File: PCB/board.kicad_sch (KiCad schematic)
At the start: 18 parts, among them SW1 SW_SPST, SW2 SW_Push, U1 STM32H743VITx, Y1 25 MHz

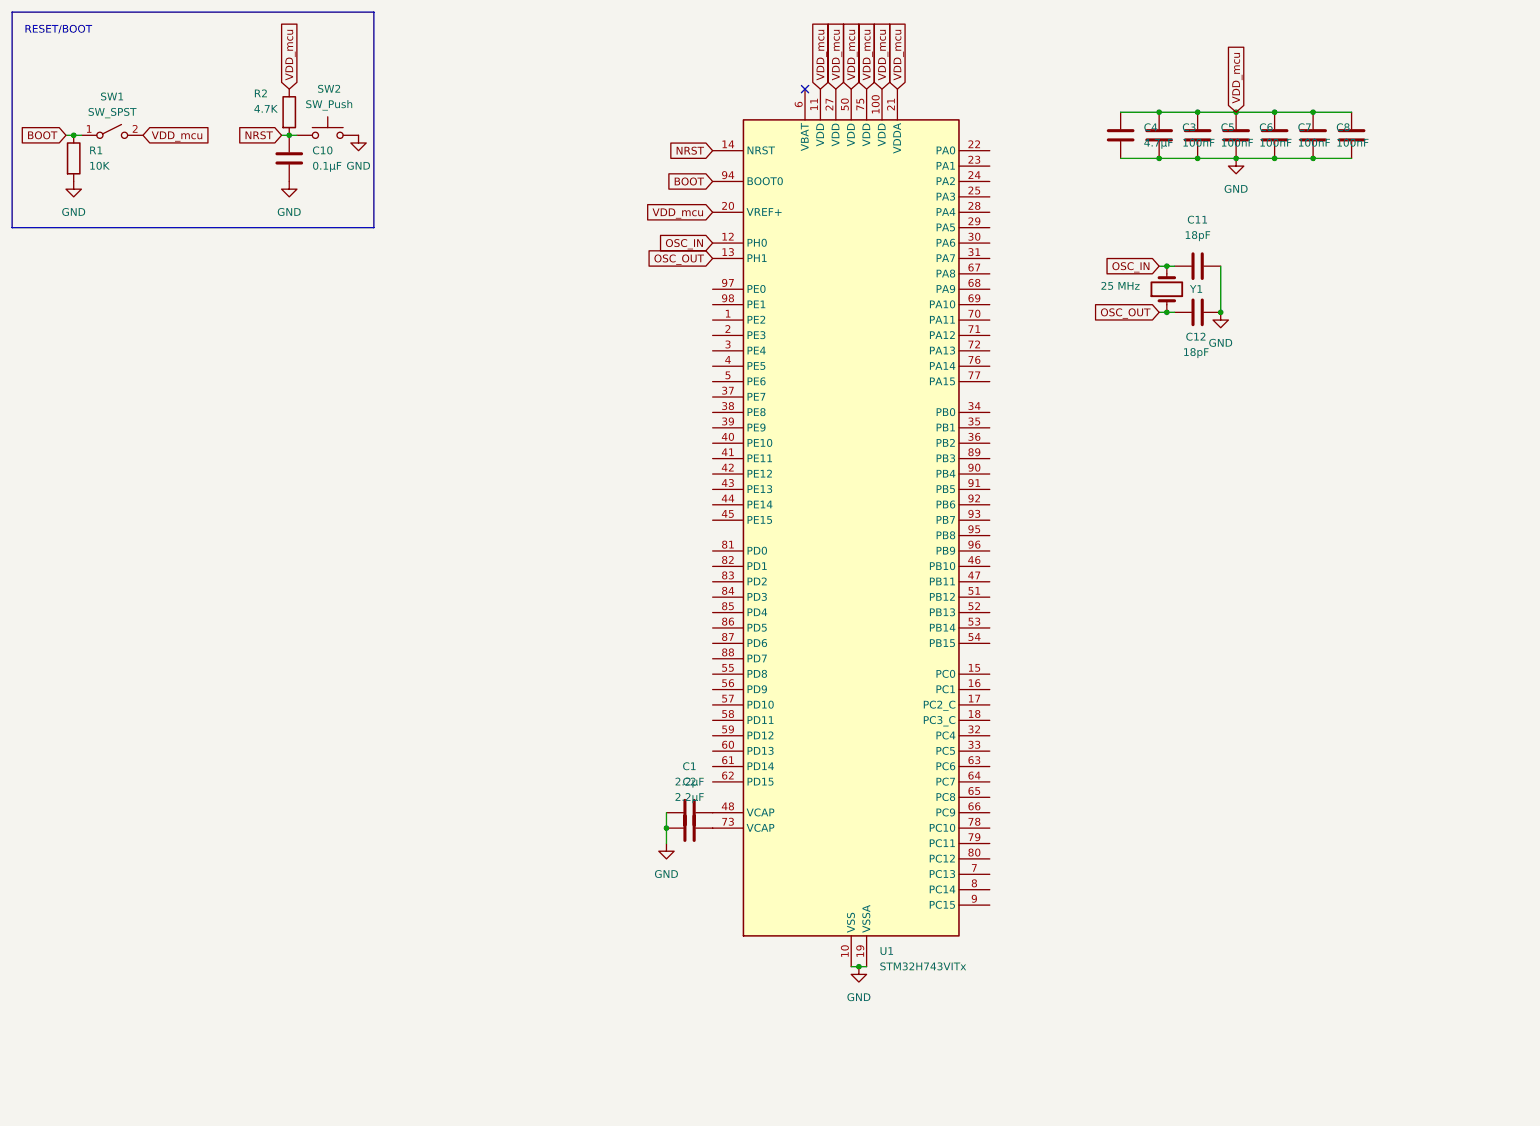
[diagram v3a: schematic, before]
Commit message: adding ferrite bead to VDD
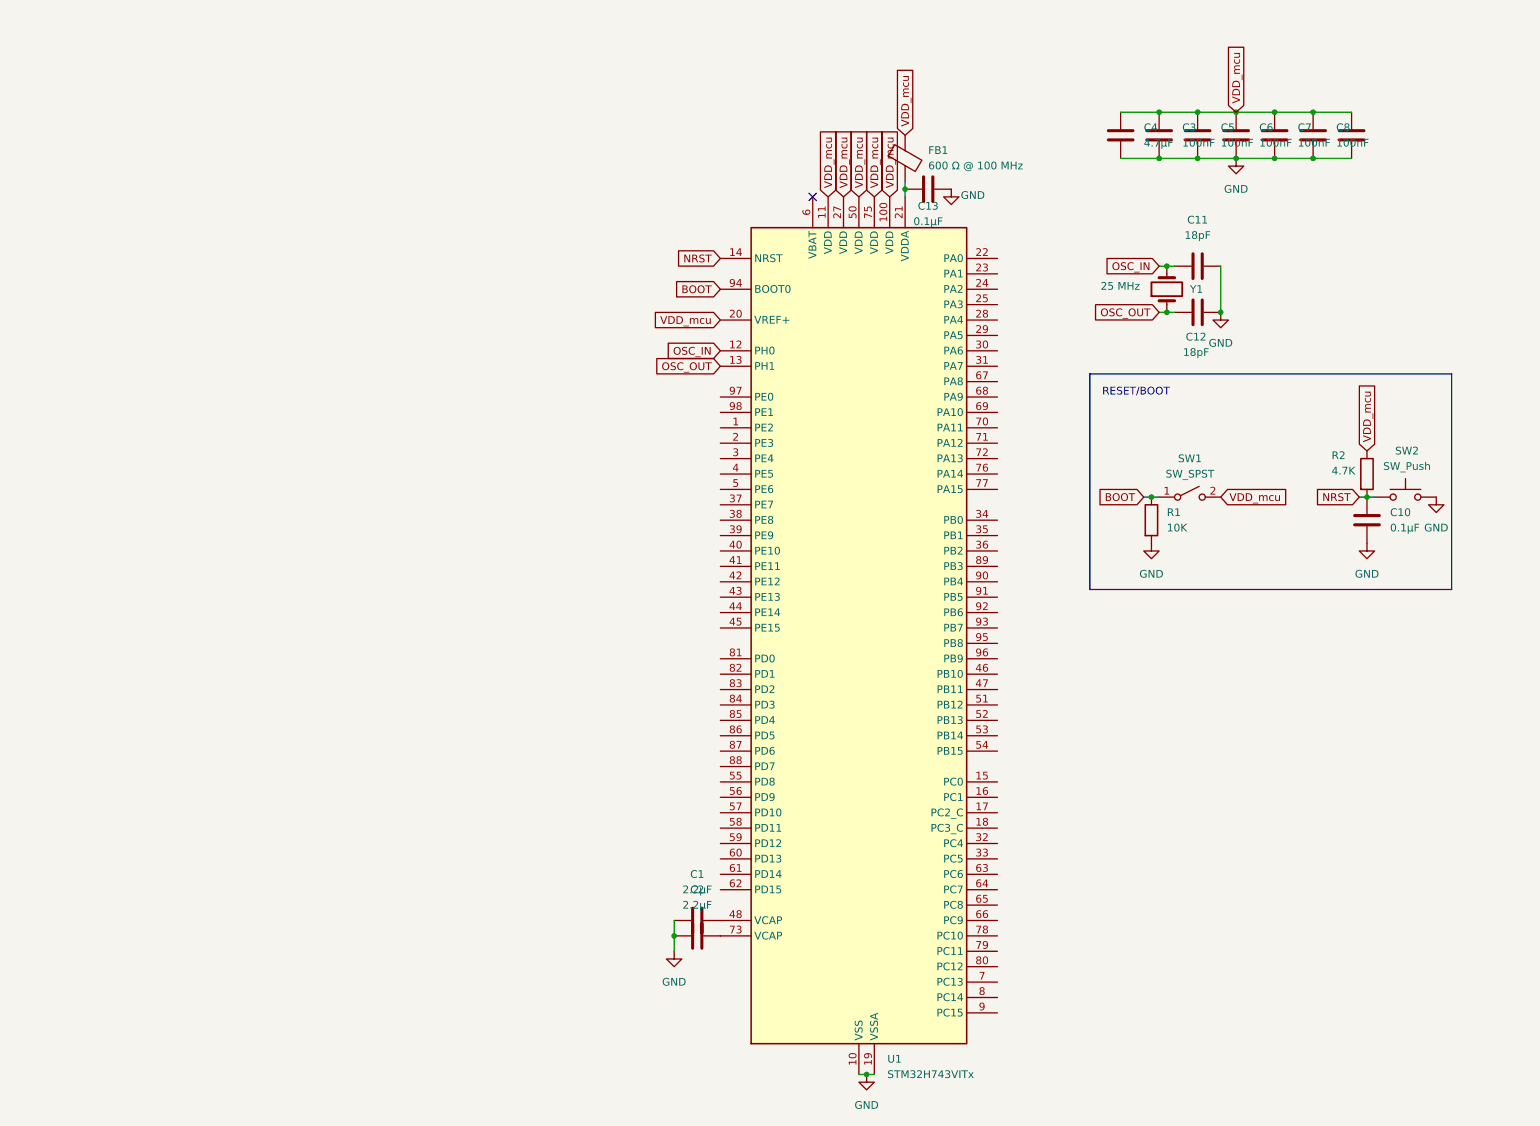
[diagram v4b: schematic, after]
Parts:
- added C13: 0.1µF, symbol Device:C
- added FB1: 600 Ω @ 100 MHz, symbol Device:FerriteBead
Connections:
- net GND: now also C13.2
- net VDD_mcu: now also FB1.1; no longer U1.21 (VDDA)
- new net: C13.1, FB1.2, U1.21 (VDDA)
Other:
- moved on the sheet: C1, C10, C2, R1, R2, SW1, SW2, U1

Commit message: adding my SWD debugger headers, I think I'm using the wrong symbol though
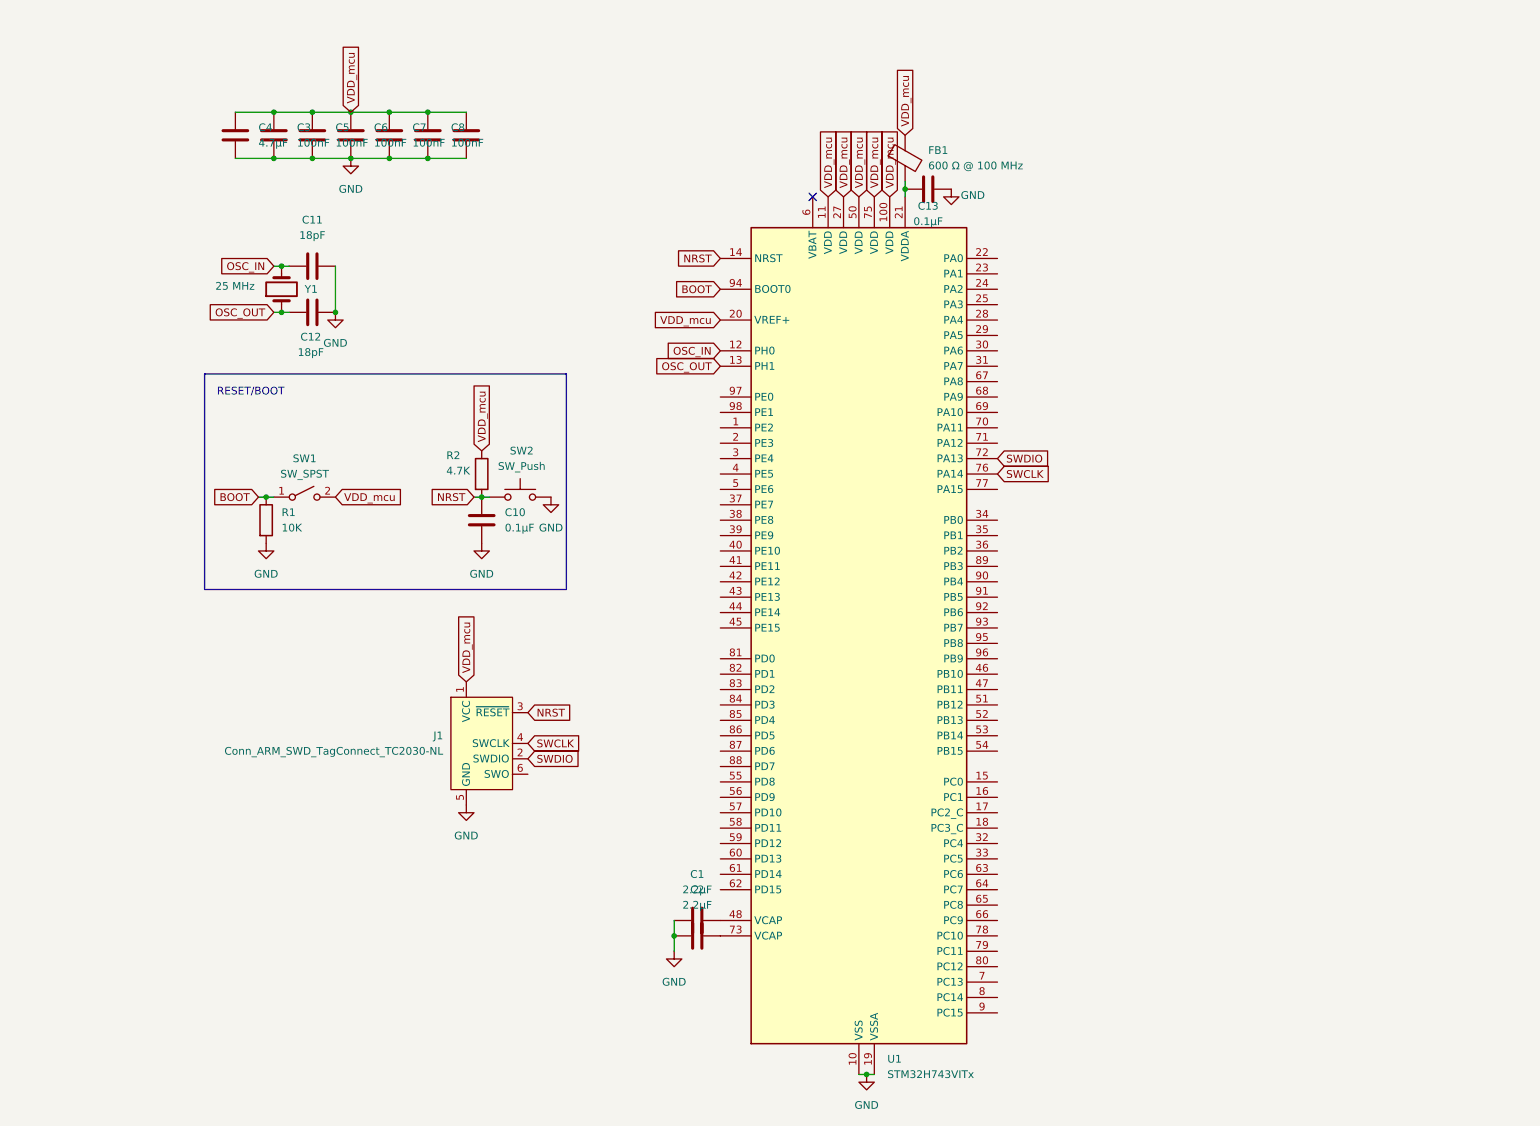
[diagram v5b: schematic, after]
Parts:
- added J1: Conn_ARM_SWD_TagConnect_TC2030-NL, Connector:Tag-Connect_TC2030-IDC-NL_2x03_P1.27mm_Vertical, symbol Connector:Conn_ARM_SWD_TagConnect_TC2030-NL
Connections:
- net GND: now also J1.5 (GND)
- net NRST: now also J1.3 (~{RESET})
- net VDD_mcu: now also J1.1 (VCC)
- net SWDIO: now reaches U1.72 (PA13)
- net SWDIO: now also J1.2 (SWDIO)
- net SWCLK: now reaches U1.76 (PA14)
- net SWCLK: now also J1.4 (SWCLK)
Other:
- moved on the sheet: C10, C11, C12, C3, C4, C5, C6, C7, C8, R1, R2, SW1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

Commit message: added the JTAG/SWD connector, and made it more detailed
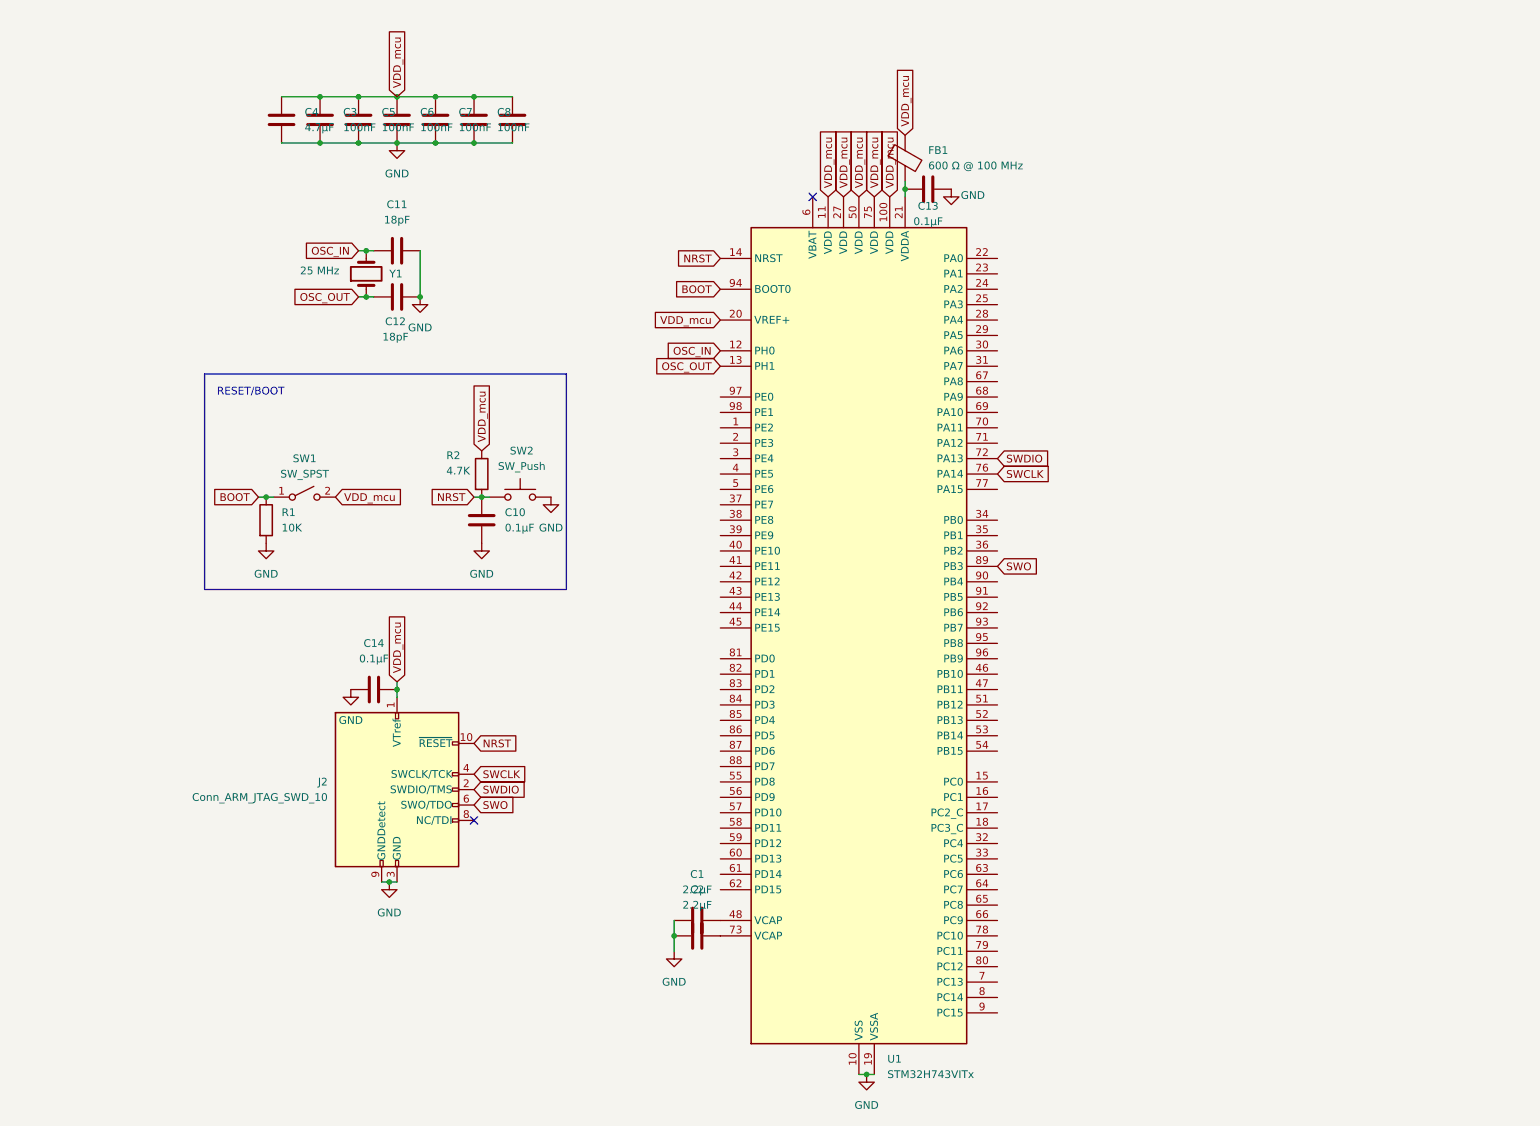
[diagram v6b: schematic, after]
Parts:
- removed J1: Conn_ARM_SWD_TagConnect_TC2030-NL, Connector:Tag-Connect_TC2030-IDC-NL_2x03_P1.27mm_Vertical, symbol Connector:Conn_ARM_SWD_TagConnect_TC2030-NL
- added C14: 0.1µF, symbol Device:C
- added J2: Conn_ARM_JTAG_SWD_10, symbol Connector:Conn_ARM_JTAG_SWD_10
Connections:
- net GND: now also C14.1, J2.3 (GND), J2.5 (GND), J2.9 (GNDDetect)
- net NRST: now also J2.10 (~{RESET})
- net SWCLK: now also J2.4 (SWCLK/TCK)
- net SWDIO: now also J2.2 (SWDIO/TMS)
- net VDD_mcu: now also C14.2, J2.1 (VTref)
- net SWO: now reaches U1.89 (PB3)
- net SWO: now also J2.6 (SWO/TDO)
- no-connect marks 1 -> 2
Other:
- moved on the sheet: C11, C12, C3, C4, C5, C6, C7, C8, Y1

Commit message: adding the SD card
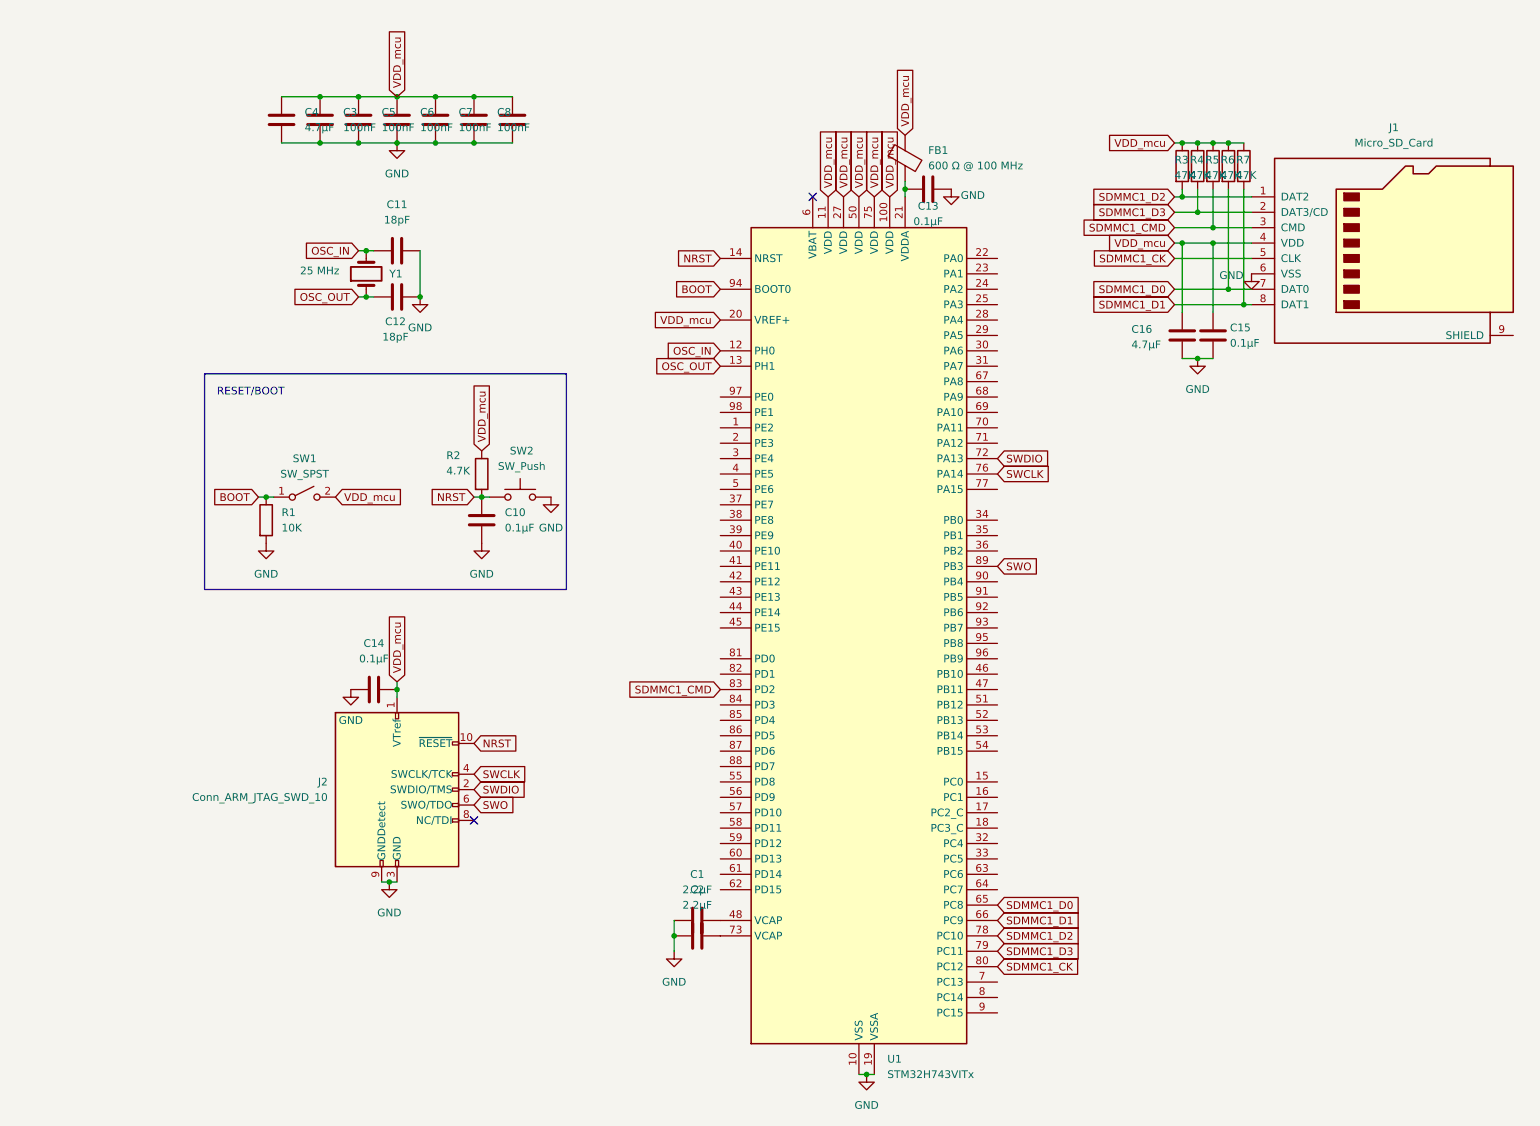
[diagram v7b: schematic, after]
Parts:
- added C15: 0.1µF, symbol Device:C
- added C16: 4.7µF, symbol Device:C
- added J1: Micro_SD_Card, symbol Connector:Micro_SD_Card
- added R3, R4, R5, R6, R7: 47K, symbol Device:R
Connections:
- net GND: now also C15.2, C16.2, J1.6 (VSS)
- net VDD_mcu: now also C15.1, C16.1, J1.4 (VDD), R3.1, R4.1, R5.1, R6.1, R7.1
- net SDMMC1_D0: now reaches U1.65 (PC8)
- net SDMMC1_D0: now also J1.7 (DAT0), R6.2
- net SDMMC1_D1: now reaches U1.66 (PC9)
- net SDMMC1_D1: now also J1.8 (DAT1), R7.2
- net SDMMC1_D2: now reaches U1.78 (PC10)
- net SDMMC1_D2: now also J1.1 (DAT2), R3.2
- net SDMMC1_D3: now reaches U1.79 (PC11)
- net SDMMC1_D3: now also J1.2 (DAT3/CD), R4.2
- net SDMMC1_CK: now reaches U1.80 (PC12)
- net SDMMC1_CK: now also J1.5 (CLK)
- net SDMMC1_CMD: now reaches U1.83 (PD2)
- net SDMMC1_CMD: now also J1.3 (CMD), R5.2

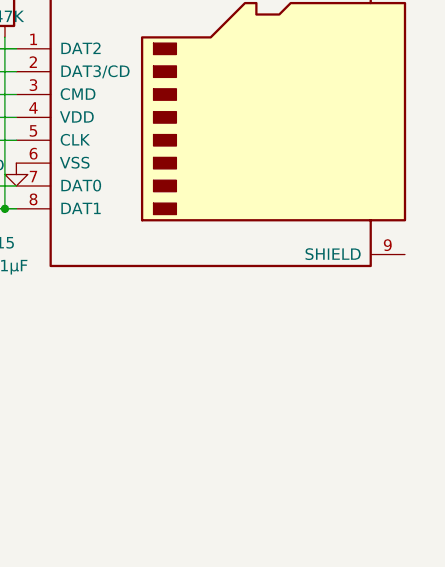
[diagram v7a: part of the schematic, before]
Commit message: connected shield to GND and updated journal with SD card
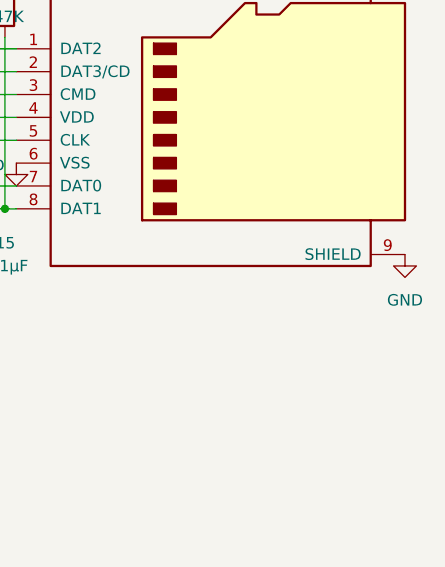
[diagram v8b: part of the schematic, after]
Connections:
- net GND: now also J1.9 (SHIELD)
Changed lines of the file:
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@@
+	)
+	(symbol
+		(lib_id "power:GND")
+		(at 260.35 66.04 0)
+		(unit 1)
+		(exclude_from_sim no)
+		(in_bom yes)
+		(on_board yes)
+		(dnp no)
+		(fields_autoplaced yes)
+		(property "Reference" "#PWR013"
+			(at 260.35 72.39 0)
+			(effects
+				(font
+					(size 1.27 1.27)
+				)
+				(hide yes)
+			)
+		)
+		(property "Value" "GND"
+			(at 260.35 71.12 0)
+			(effects
+				(font
+					(size 1.27 1.27)
+				)
+			)
+		)
+		(property "Footprint" ""
+			(at 260.35 66.04 0)
+			(effects
+				(font
+					(size 1.27 1.27)
+				)
+				(hide yes)
+			)
+		)
+		(property "Datasheet" ""
+			(at 260.35 66.04 0)
+			(effects
+				(font
+					(size 1.27 1.27)
+				)
+				(hide yes)
+			)
+		)
+		(property "Description" "Power symbol creates a global label with name \"GND\" , ground"
+			(at 260.35 66.04 0)
+			(effects
+				(font
+					(size 1.27 1.27)
+				)
+				(hide yes)
+			)
+		)
+		(pin "1"
+		)
+		(instances
+			(project ""
+				(path "/93bdda59-fc0f-4b76-8be9-fa93964bed43"
+					(reference "#PWR013")
+					(unit 1)
+				)
+			)
+		)
 	)
 	(symbol
